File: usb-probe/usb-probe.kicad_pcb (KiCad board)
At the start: 2 copper layers, 5 parts, among them J1 USB_C_Receptacle, J2 Conn_02x09_Top_Bottom, J3 USB_C_Receptacle

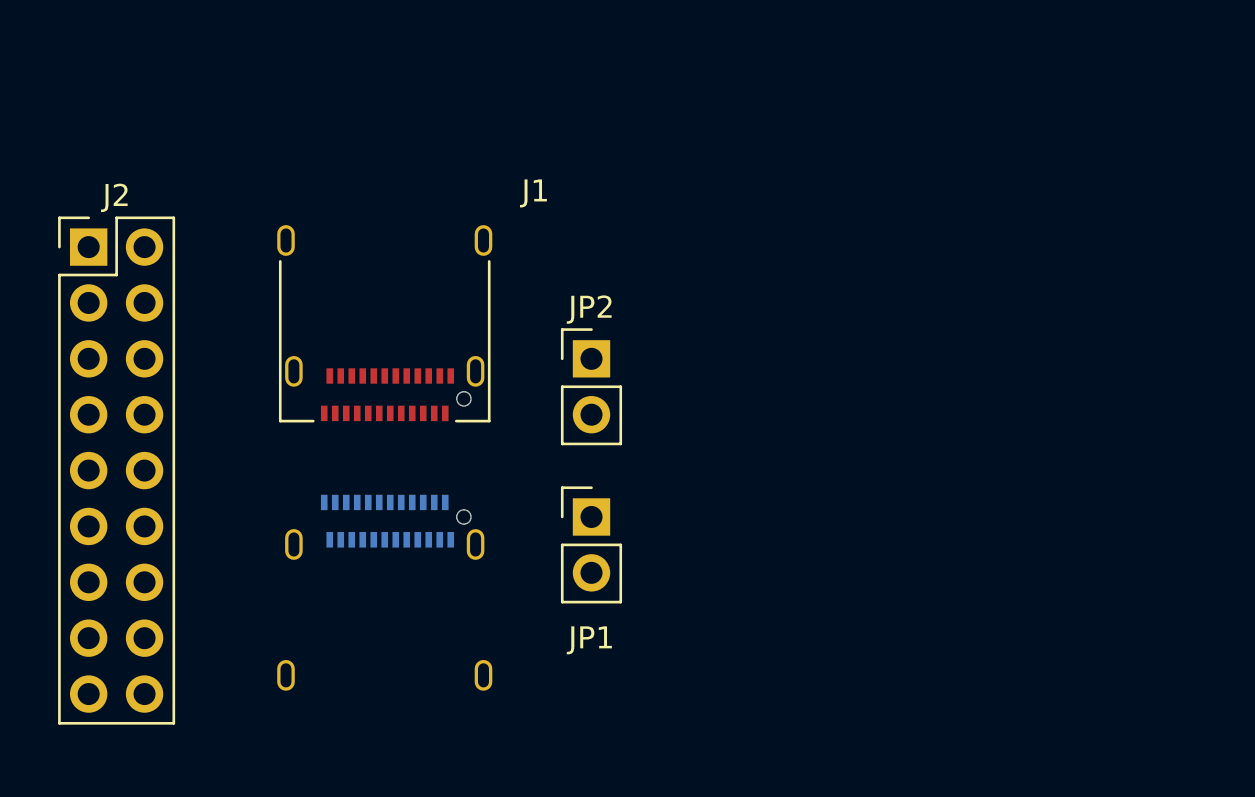
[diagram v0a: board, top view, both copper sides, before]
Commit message: Started routing PCB
And fixed an accidental connection in the schema.
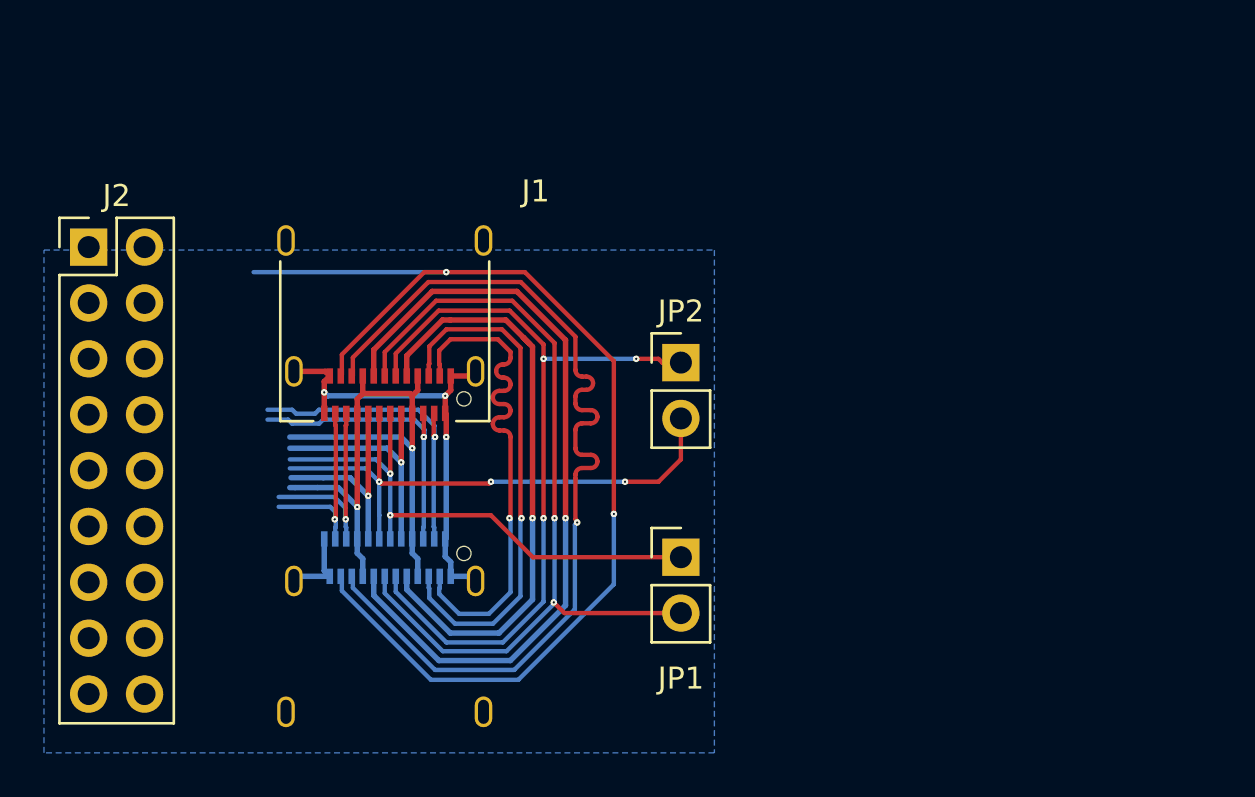
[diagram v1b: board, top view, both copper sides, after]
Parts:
- moved JP1 4.46 mm to (143.8, 72.5)
- moved JP2 4.07 mm to (143.8, 63.7)
- moved J3 1.66 mm to (130.3, 76.7)
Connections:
- J1 pad A3: /RX2+ -> /TX1-
- J2 pad 16: /RX2+ -> /TX1-
- J3 pad A3: /RX2+ -> /TX1-
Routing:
- net /TX2+: track 0.00 -> 52.0 mm, vias 0 -> 2
- net /TX2-: track 0.00 -> 43.2 mm, vias 0 -> 1
- net /B-D+: track 0.00 -> 38.9 mm, vias 0 -> 2
- net /B-D-: track 0.00 -> 36.3 mm, vias 0 -> 3
- net /CC2: track 0.00 -> 35.8 mm, vias 0 -> 1
- net /VBUS: track 0.00 -> 30.1 mm, vias 0 -> 2
- net /SBU2: track 0.00 -> 27.5 mm, vias 0 -> 1
- net /A-D-: track 0.00 -> 26.1 mm, vias 0 -> 3
- net /A-D+: track 0.00 -> 24.5 mm, vias 0 -> 2
- net GND: track 0.00 -> 24.4 mm, vias 0 -> 3
- net /RX1-: track 0.00 -> 23.6 mm, vias 0 -> 1
- net /RX1+: track 0.00 -> 23.5 mm, vias 0 -> 1
- net /TX1+: track 0.00 -> 14.3 mm, vias 0 -> 1
- net /TX1-: track 0.00 -> 13.6 mm, vias 0 -> 1
- net /CC1: track 0.00 -> 11.0 mm, vias 0 -> 1
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- added copper zone on B.Cu, net GND

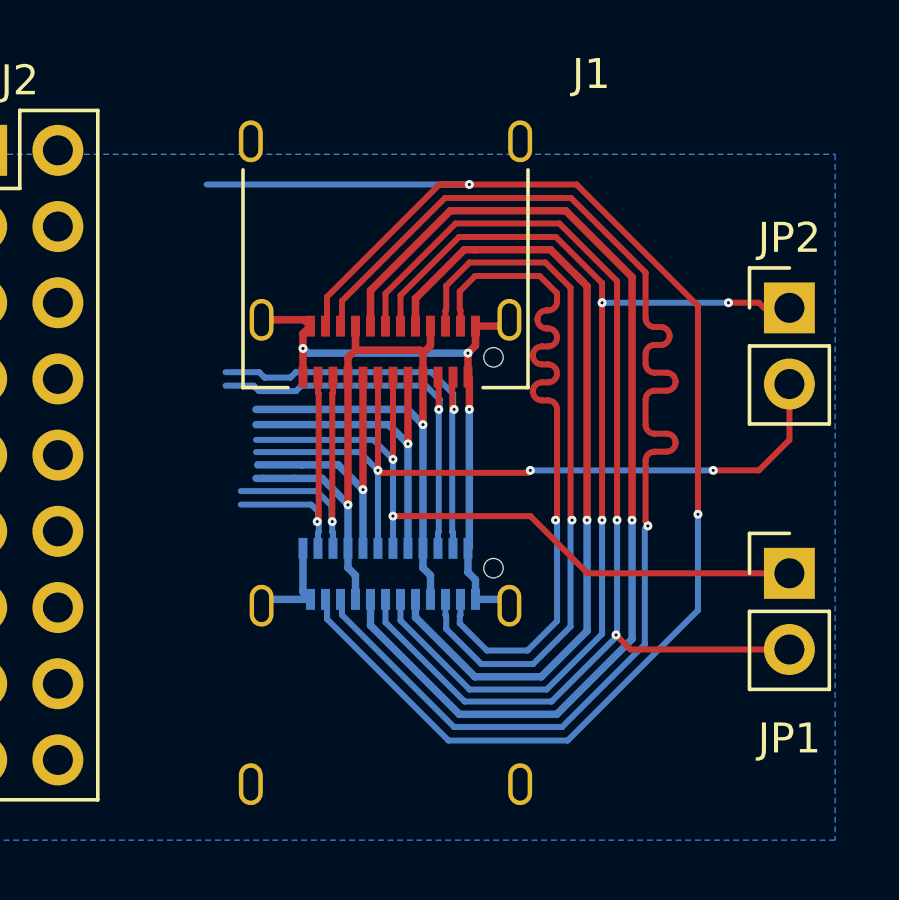
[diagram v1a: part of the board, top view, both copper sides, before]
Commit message: Added vias for B pin header
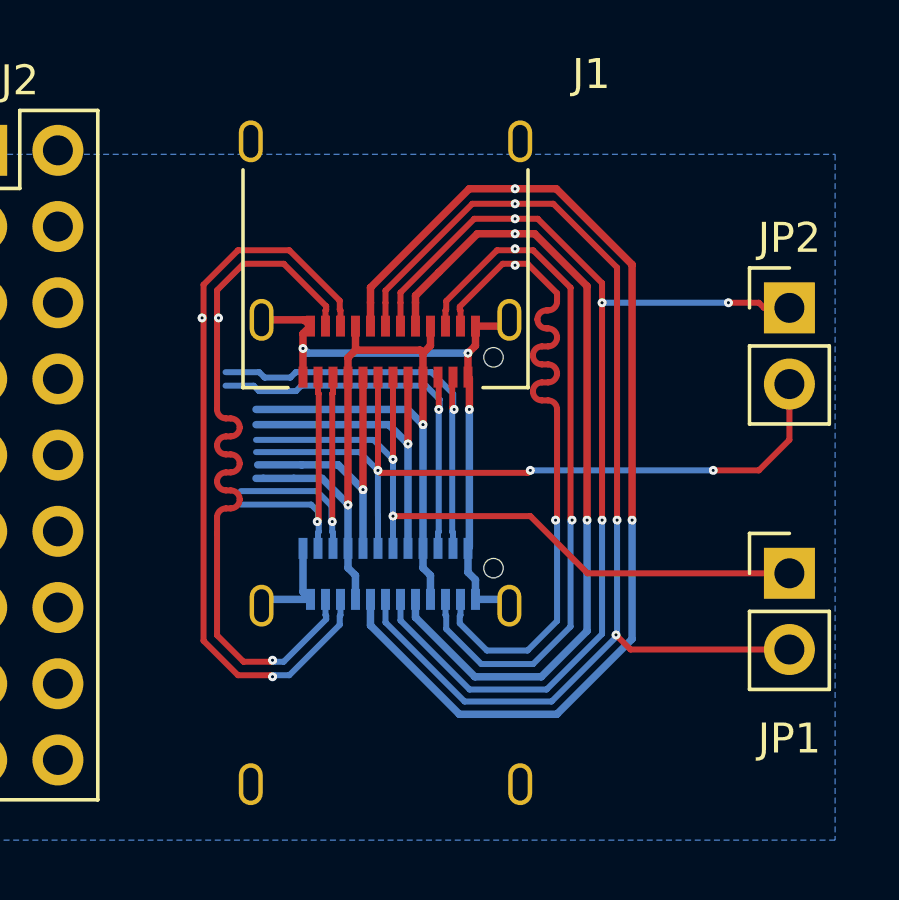
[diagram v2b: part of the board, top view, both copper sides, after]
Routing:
- net /TX2+: track 52.0 -> 25.2 mm
- net /TX2-: track 43.2 -> 25.4 mm, vias 1 -> 2
- net /CC2: track 35.8 -> 36.8 mm, vias 1 -> 2
- net /B-D+: track 38.9 -> 39.7 mm, vias 2 -> 3
- net /B-D-: track 36.3 -> 36.9 mm, vias 3 -> 4
- net /SBU2: track 27.5 -> 27.6 mm, vias 1 -> 2
- net /RX1-: track 23.6 -> 23.7 mm, vias 1 -> 2
- net /RX1+: track 23.5 -> 23.6 mm, vias 1 -> 2

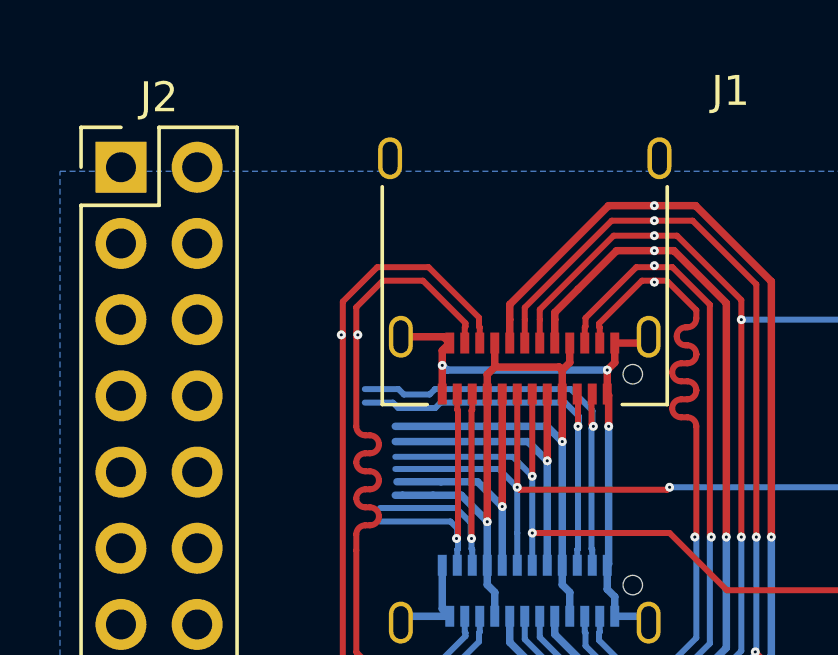
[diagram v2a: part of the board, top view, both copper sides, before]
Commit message: Routed B-side to pin header
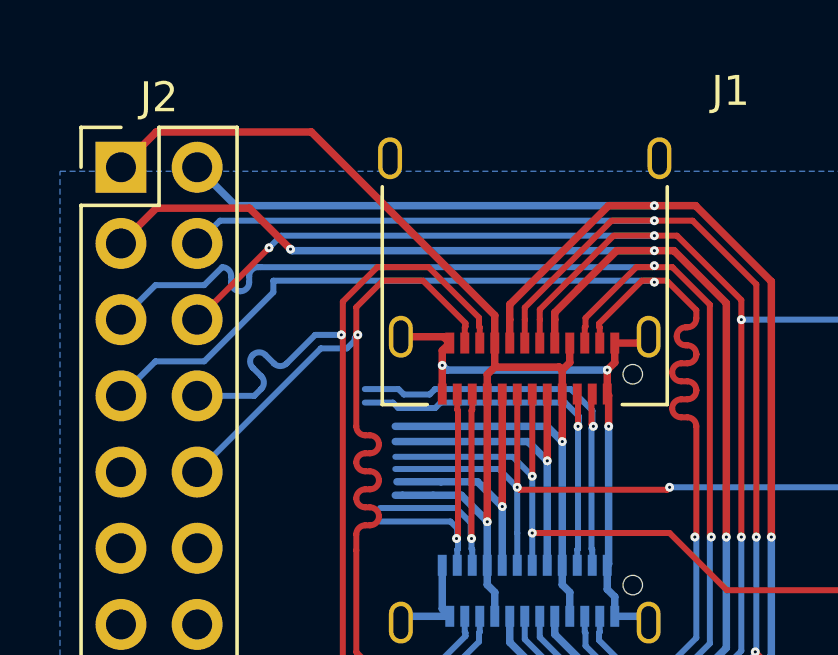
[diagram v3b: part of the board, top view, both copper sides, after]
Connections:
- J2 pad 1: /RX1+ -> /VBUS
- J2 pad 10: /RX2+ -> /TX2+
- J2 pad 11: /RX2- -> unconnected-(J2-Pin_11-Pad11)
- J2 pad 12: /SBU1 -> unconnected-(J2-Pin_12-Pad12)
- J2 pad 13: /A-D- -> unconnected-(J2-Pin_13-Pad13)
- J2 pad 14: /A-D+ -> unconnected-(J2-Pin_14-Pad14)
- J2 pad 15: /CC1 -> unconnected-(J2-Pin_15-Pad15)
- J2 pad 16: /TX1- -> unconnected-(J2-Pin_16-Pad16)
- J2 pad 17: /TX1+ -> unconnected-(J2-Pin_17-Pad17)
- J2 pad 2: /RX1- -> /CC2
- J2 pad 4: /B-D- -> /B-D+
- J2 pad 5: /B-D+ -> /RX1-
- J2 pad 6: /CC2 -> /B-D-
- J2 pad 7: /TX2- -> /RX1+
- J2 pad 8: /TX2+ -> /TX2-
- J2 pad 9: /VBUS -> unconnected-(J2-Pin_9-Pad9)
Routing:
- net /RX1+: track 23.6 -> 43.2 mm
- net /RX1-: track 23.7 -> 43.3 mm
- net /SBU2: track 27.6 -> 46.4 mm, vias 2 -> 3
- net /VBUS: track 30.1 -> 46.5 mm
- net /B-D-: track 36.9 -> 53.3 mm, vias 4 -> 5
- net /CC2: track 36.8 -> 52.5 mm
- net /B-D+: track 39.7 -> 55.3 mm
- net /TX2+: track 25.2 -> 32.5 mm
- net /TX2-: track 25.4 -> 32.5 mm

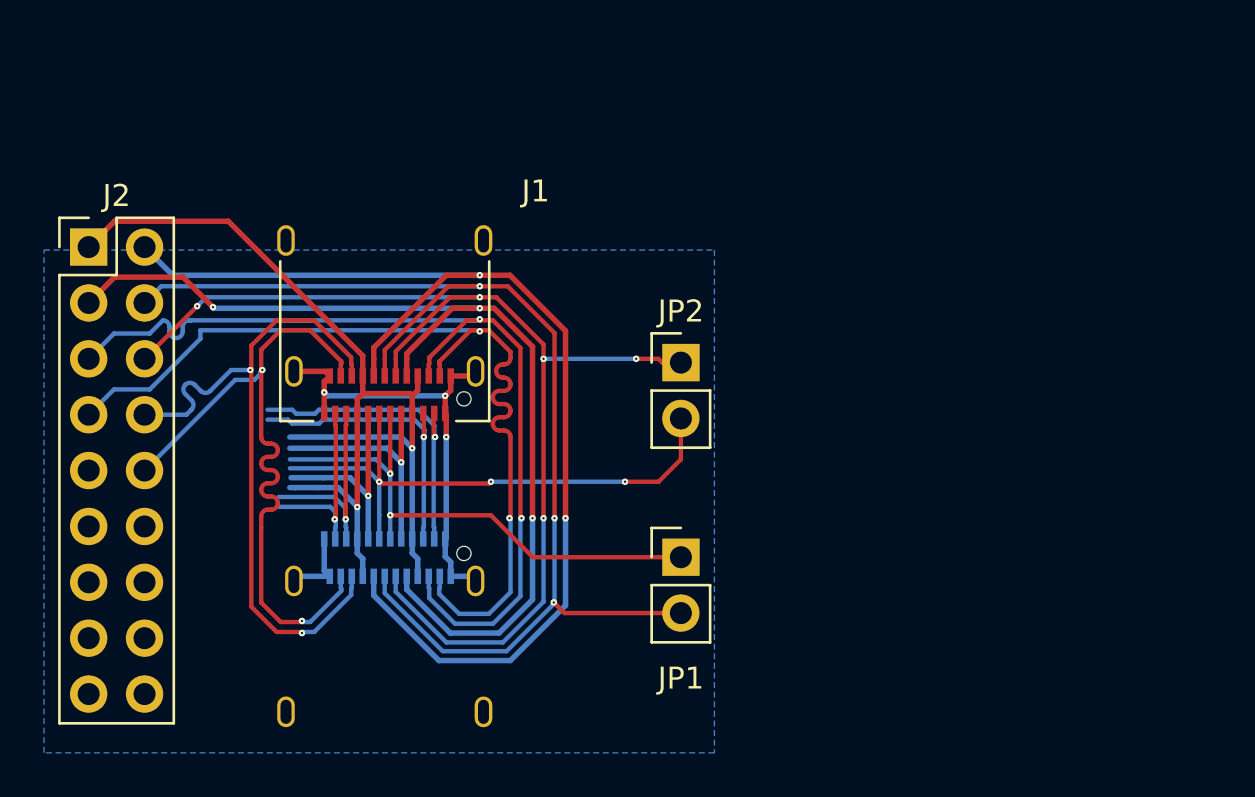
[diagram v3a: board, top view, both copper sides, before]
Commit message: Switched to USB-C Plug
I learned that USB-C cables have chips that encode their capabilities, so
putting two in series probably won't work. I've replaced one receptacle with a
plug.

I've also changed the pin header to an IDC connector, which should match what
my logic analyzer uses. By placing it between the USB-C plug and receptacle,
the routing becomes significantly simpler.
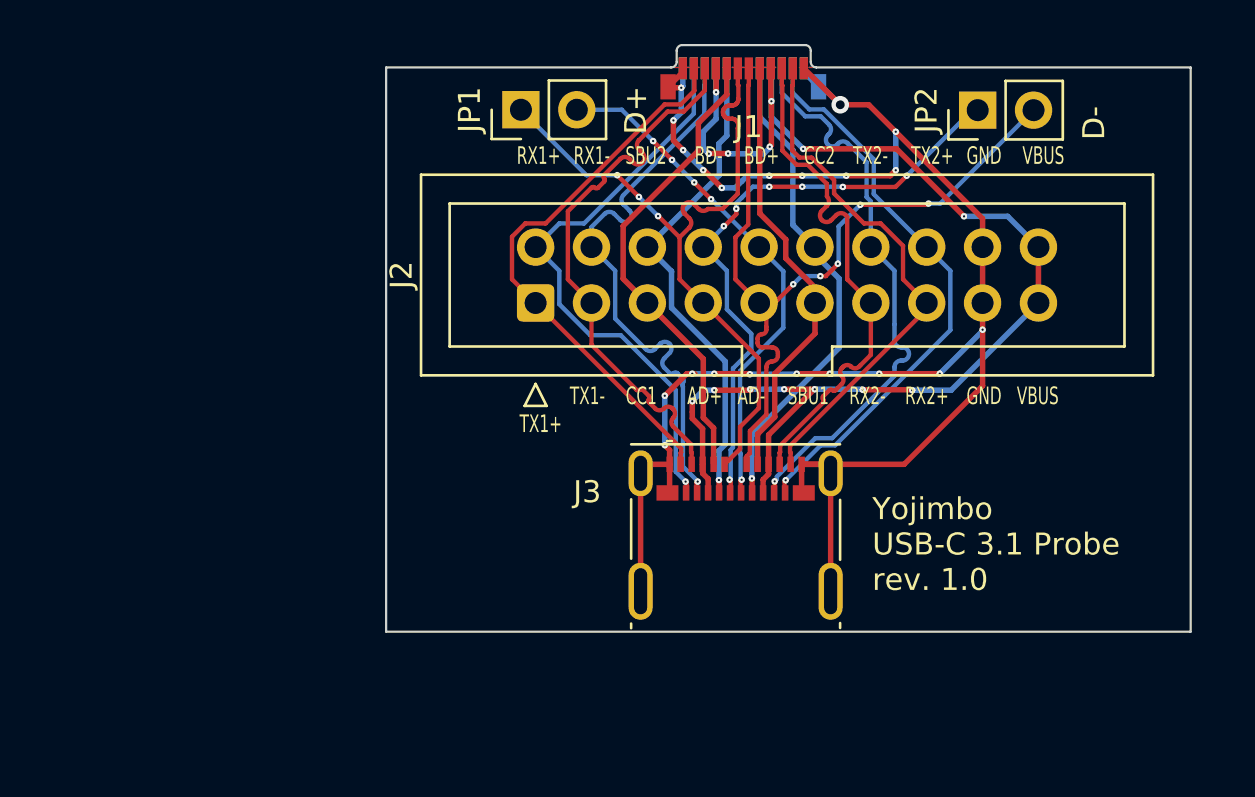
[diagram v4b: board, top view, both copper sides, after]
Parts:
- J1: value USB_C_Receptacle -> USB_C_Plug; footprint Connector_USB:USB_C_Receptacle_Amphenol_12401610E4-2A -> Connector_USB:USB_C_Plug_Molex_105444
- J2: footprint Connector_PinHeader_2.54mm:PinHeader_2x09_P2.54mm_Vertical -> Connector_IDC:IDC-Header_2x10_P2.54mm_Vertical
- J3: footprint Connector_USB:USB_C_Receptacle_Amphenol_12401610E4-2A -> Connector_USB:USB_C_Receptacle_Molex_105450-0101; moved to F.Cu
- moved JP1 21.6 mm to (136.5, 52.2), turned to 90 degrees
- moved J2 20.5 mm to (137.2, 61.0), turned to 90 degrees
- moved J1 19.5 mm to (146.6, 50.3), turned to 0 degrees
- moved JP2 17.7 mm to (157.3, 52.2), turned to 90 degrees
- moved J3 16.8 mm to (146.3, 71.5), turned to 0 degrees
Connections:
- J2 pad 1: /VBUS -> /TX1+
- J2 pad 10: /TX2+ -> /B-D+
- J2 pad 11: unconnected-(J2-Pin_11-Pad11) -> /SBU1
- J2 pad 12: unconnected-(J2-Pin_12-Pad12) -> /CC2
- J2 pad 13: unconnected-(J2-Pin_13-Pad13) -> /RX2-
- J2 pad 14: unconnected-(J2-Pin_14-Pad14) -> /TX2-
- J2 pad 15: unconnected-(J2-Pin_15-Pad15) -> /RX2+
- J2 pad 16: unconnected-(J2-Pin_16-Pad16) -> /TX2+
- J2 pad 17: unconnected-(J2-Pin_17-Pad17) -> GND
- J2 pad 2: /CC2 -> /RX1+
- J2 pad 3: /SBU2 -> /TX1-
- J2 pad 4: /B-D+ -> /RX1-
- J2 pad 5: /RX1- -> /CC1
- J2 pad 6: /B-D- -> /SBU2
- J2 pad 7: /RX1+ -> /A-D+
- J2 pad 8: /TX2- -> /B-D-
- J2 pad 9: unconnected-(J2-Pin_9-Pad9) -> /A-D-
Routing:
- net GND: track 24.4 -> 84.3 mm, vias 3 -> 21
- net /B-D+: track 55.3 -> 23.4 mm, vias 3 -> 5
- net /CC2: track 52.5 -> 22.4 mm, vias 2 -> 1
- net /B-D-: track 53.3 -> 28.1 mm, vias 5 -> 7
- net /SBU2: track 46.4 -> 22.4 mm, vias 3 -> 1
- net /RX1-: track 43.3 -> 26.5 mm, vias 2 -> 1
- net /RX1+: track 43.2 -> 26.6 mm, vias 2 -> 1
- net /RX2+: track 8.82 -> 23.9 mm, vias 1 -> 0
- net /RX2-: track 9.53 -> 23.7 mm, vias 1 -> 0
- net /VBUS: track 46.5 -> 59.2 mm, vias 2 -> 14
- net /TX1-: track 13.6 -> 25.5 mm, vias 1 -> 0
- net /A-D-: track 26.1 -> 37.7 mm, vias 3 -> 5
- net /TX1+: track 14.3 -> 25.6 mm, vias 1 -> 0
- net /CC1: track 11.0 -> 21.7 mm, vias 1 -> 0
- net /SBU1: track 9.56 -> 20.1 mm, vias 1 -> 0
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- added copper zone on B.Cu, net /VBUS
- added copper zone on F.Cu, net GND
- removed copper zone on B.Cu, net GND
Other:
- board outline added: 36.6 x 26.7 mm
- board text added: "AD+"
- board text added: "AD-"
- board text added: "BD+"
- board text added: "BD-"
- board text added: "CC1"
- board text added: "CC2"
- board text added: "D+"
- board text added: "D-"
- board text added: "GND"
- board text added: "RX1+"
- board text added: "RX1-"
- board text added: "RX2+"
- board text added: "RX2-"
- board text added: "SBU1"
- board text added: "SBU2"
- board text added: "TX1+"
- board text added: "TX1-"
- board text added: "TX2+"
- board text added: "TX2-"
- board text added: "VBUS"
- board text added: "Yojimbo USB-C 3.1 Probe rev. 1.0"

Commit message: Disconnect Ground and Shield
It's up to the connected device to decide what to do with the shield, we just
need to pass it through.

Fixes #4
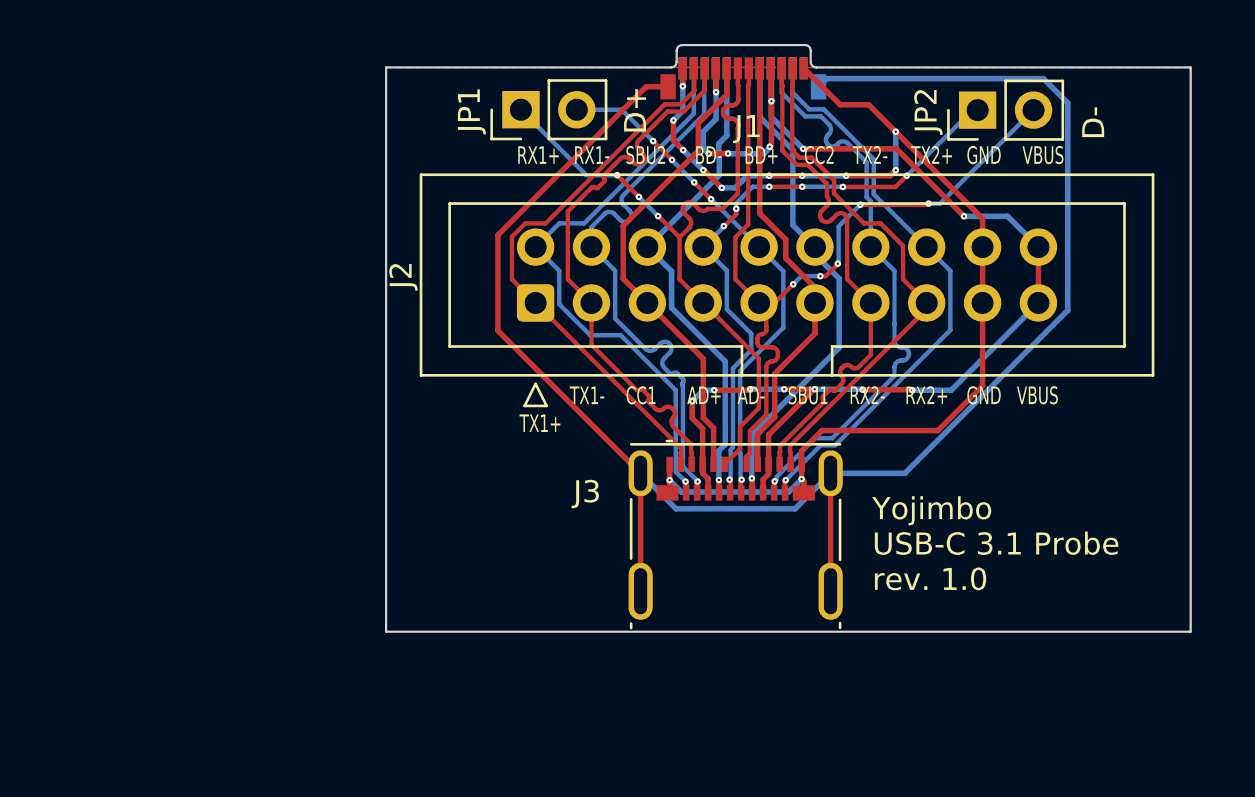
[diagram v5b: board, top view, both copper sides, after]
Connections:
- J1 pad S1: GND -> /Shield
- J3 pad S1: GND -> /Shield
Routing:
- net /Shield: track 0.00 -> 81.2 mm
- net GND: track 84.3 -> 55.3 mm, vias 21 -> 12
- added copper zone on B.Cu, net /Shield
- added copper zone on F.Cu, net /Shield
- removed copper zone on B.Cu, net /VBUS
- removed copper zone on F.Cu, net GND
